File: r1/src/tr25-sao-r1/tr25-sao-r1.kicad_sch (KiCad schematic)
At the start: 1 part

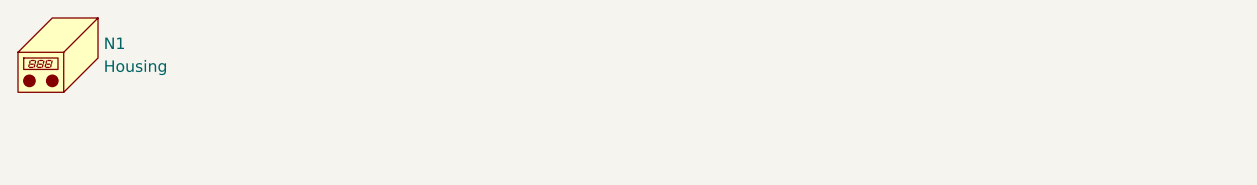
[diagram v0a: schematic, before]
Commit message: jeffmakes Kicad library as submodule
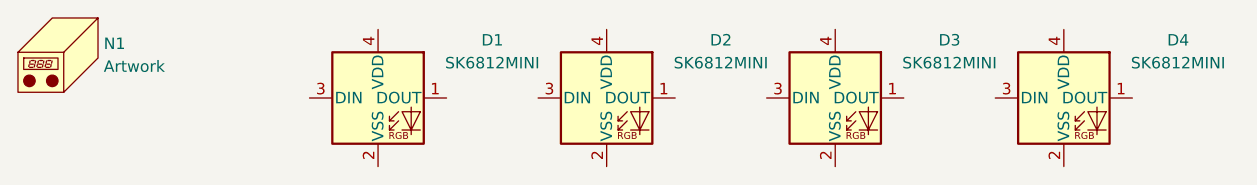
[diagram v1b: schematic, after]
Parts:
- added D1, D2, D3, D4: SK6812MINI, jeffmakes-footprints:LED_PLCC4_3.2x2.8mm_CCW, symbol LED:SK6812MINI
- N1: value Housing -> Artwork

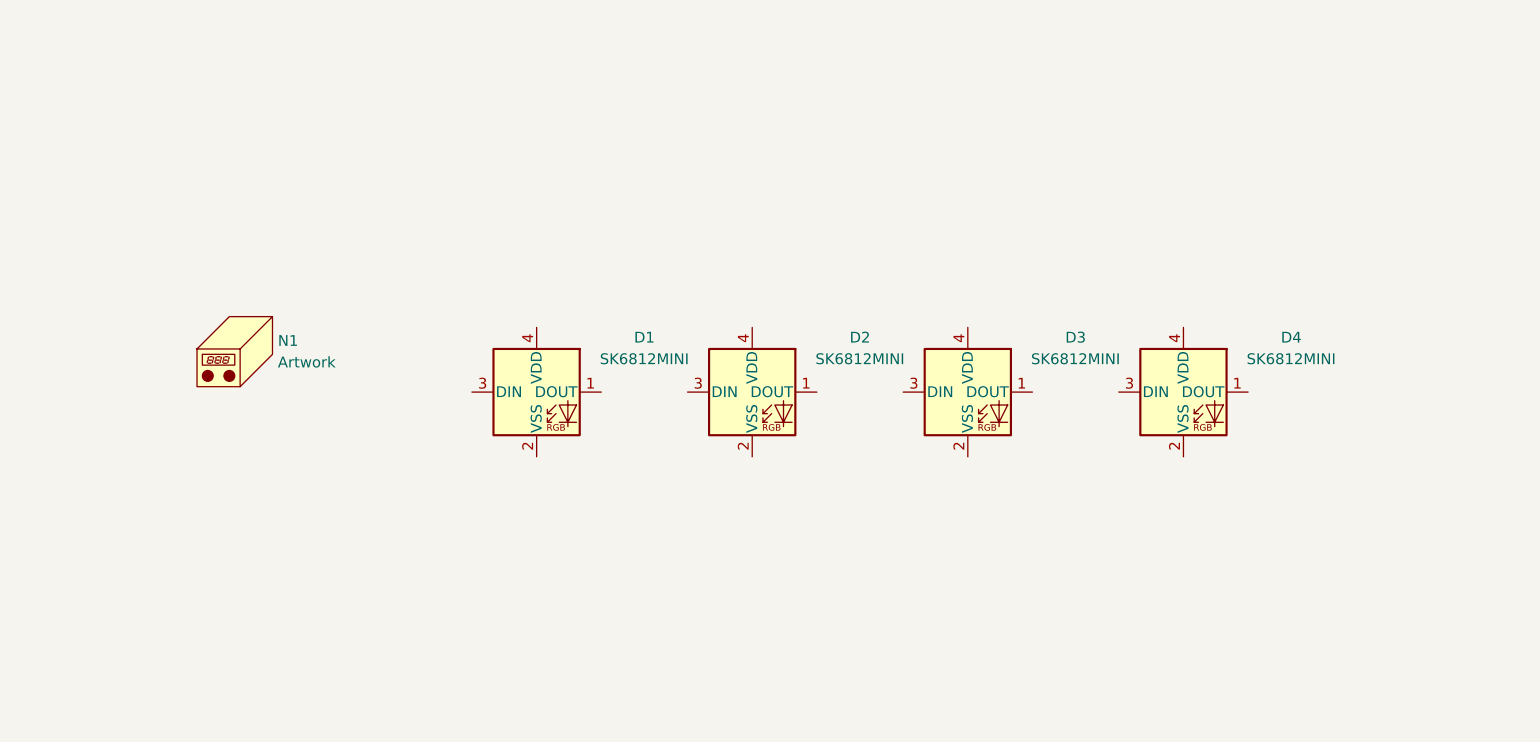
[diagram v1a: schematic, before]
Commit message: Schematic complete, ERC pass
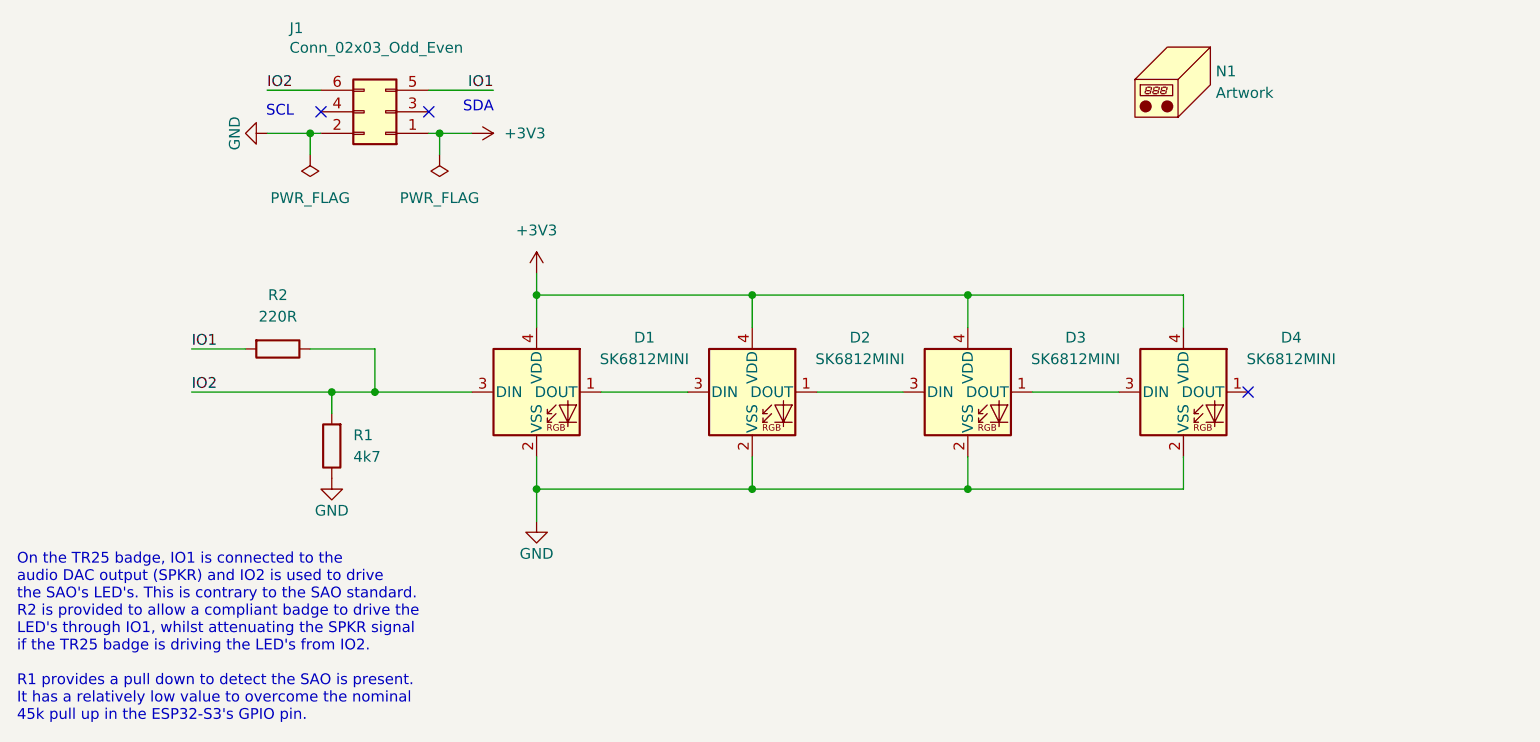
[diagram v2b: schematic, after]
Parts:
- added J1: Conn_02x03_Odd_Even, Connector_PinHeader_2.54mm:PinHeader_2x03_P2.54mm_Vertical_SMD, symbol Connector_Generic:Conn_02x03_Odd_Even
- added R1: 4k7, symbol Device:R
- added R2: 220R, symbol Device:R
- D1, D2, D3, D4: footprint jeffmakes-footprints:LED_PLCC4_3.2x2.8mm_CCW -> LED_SMD:LED_SK6812MINI_PLCC4_3.5x3.5mm_P1.75mm
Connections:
- net GND: now reaches D4.2 (VSS)
- net GND: now also D1.2 (VSS), D2.2 (VSS), D3.2 (VSS), J1.2 (Pin_2), R1.1
- net at D4.3 (DIN): now also D3.1 (DOUT)
- net +3V3: now reaches D4.4 (VDD)
- net +3V3: now also D1.4 (VDD), D2.4 (VDD), D3.4 (VDD), J1.1 (Pin_1)
- net at D1.1 (DOUT): now also D2.3 (DIN)
- net IO2: now reaches D1.3 (DIN)
- net IO2: now also J1.6 (Pin_6), R1.2, R2.1
- net at D3.3 (DIN): now also D2.1 (DOUT)
- new net IO1: J1.5 (Pin_5), R2.2
- no-connect marks 0 -> 3
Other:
- note added: "On the TR25 badge, IO1 is connected to the audio DAC output (SPKR) and IO2 is used to drive the SAO's LED's. This is contrary to the SAO standard. R2 is provided to allow a compliant badge to drive the LED's through IO1, whilst attenuating the SPKR signal if the TR25 badge is driving the LED's from IO2. R1 provides a pull down to detect the SAO is present. It has a relatively low value to overcom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"
- note added: "SCL"
- note added: "SDA"
- moved on the sheet: N1

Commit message: Assign resistor footprints
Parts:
- R1, R2: footprint (none) -> Resistor_SMD:R_1206_3216Metric
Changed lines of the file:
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@@
 			)
 		)
-		(property "Footprint" ""
+		(property "Footprint" "Resistor_SMD:R_1206_3216Metric"
 			(at 79.248 97.79 90)
 			(hide yes)
@@
 			)
 		)
-		(property "Footprint" ""
+		(property "Footprint" "Resistor_SMD:R_1206_3216Metric"
 			(at 71.12 84.582 90)
 			(hide yes)

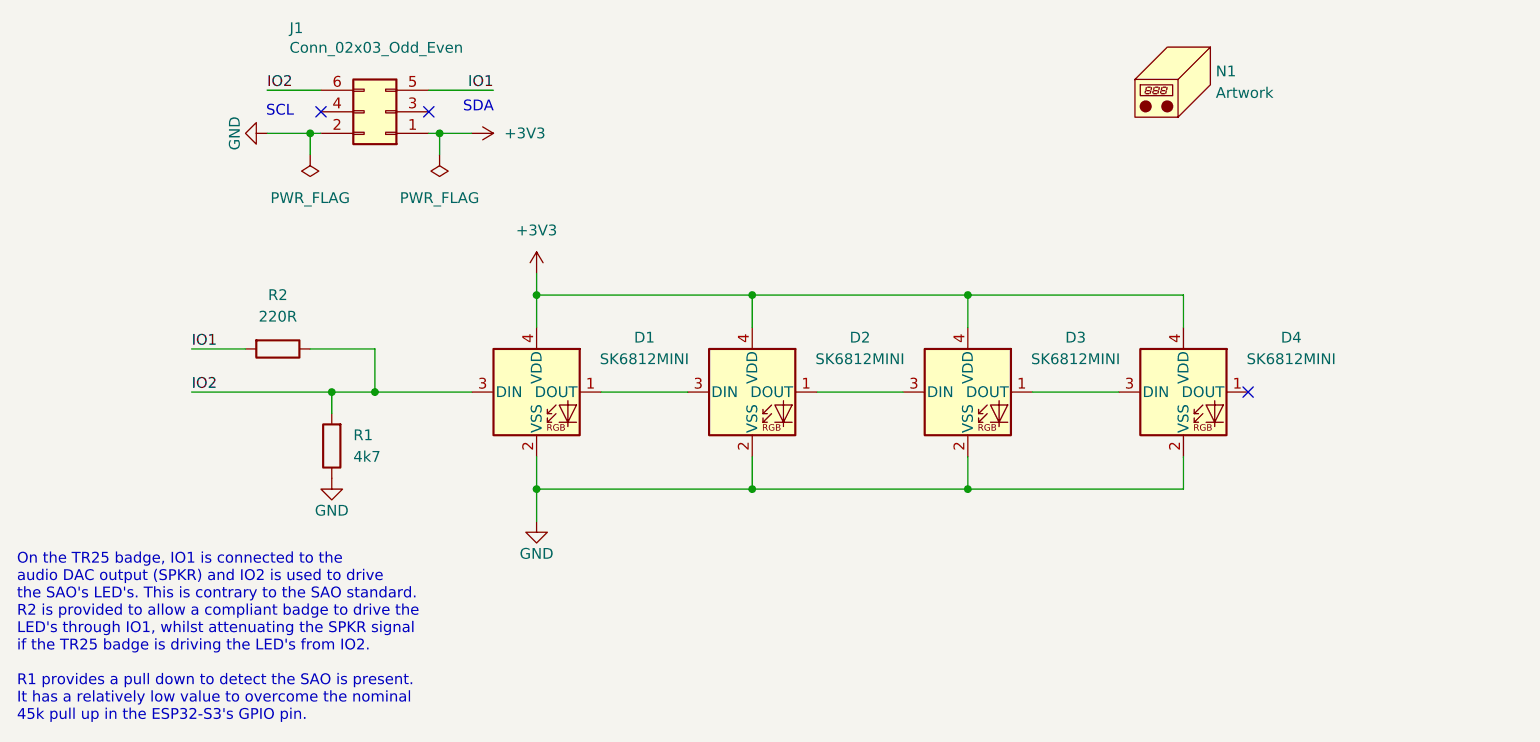
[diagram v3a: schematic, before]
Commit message: Correct LED pinout
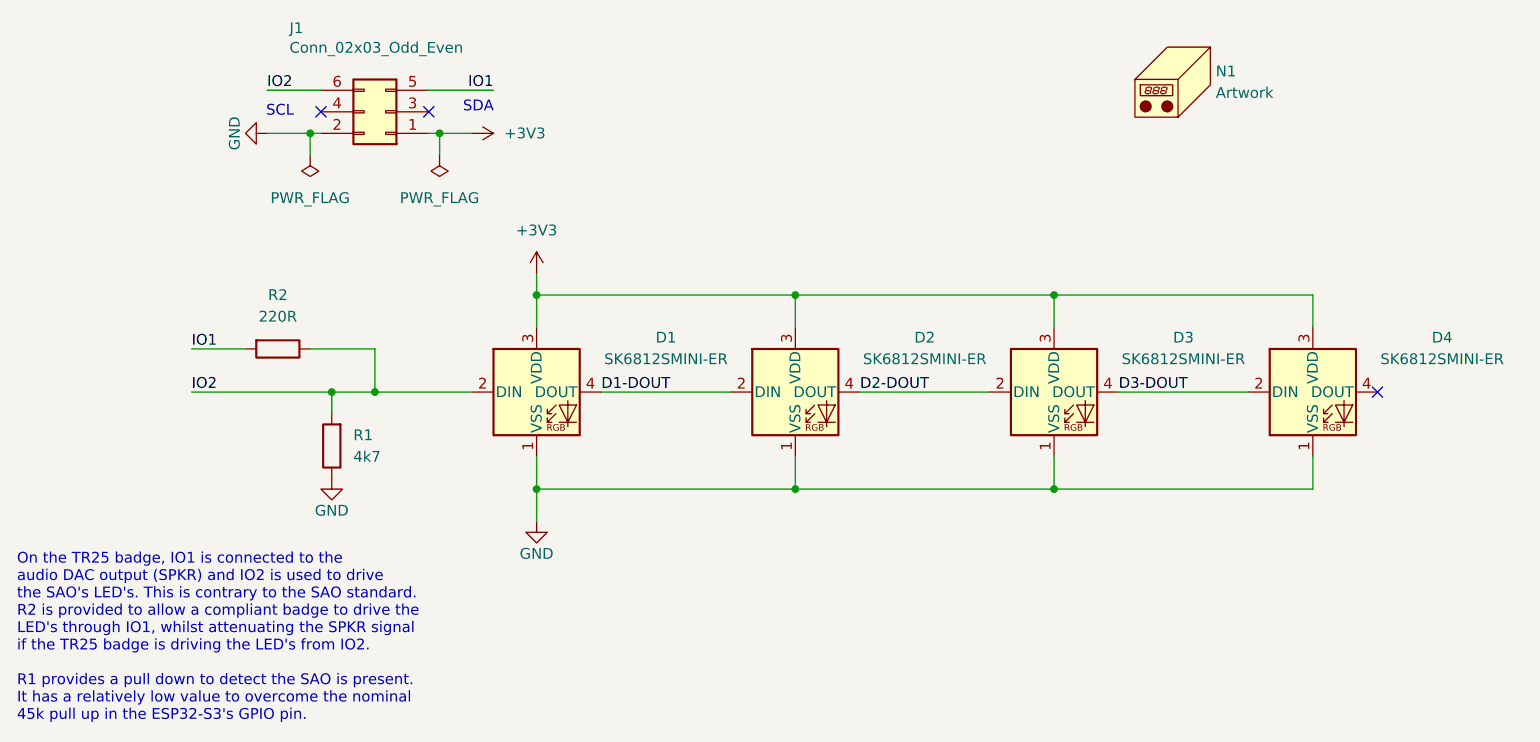
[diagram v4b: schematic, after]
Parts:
- D1, D2, D3, D4: value SK6812MINI -> SK6812SMINI-ER; footprint LED_SMD:LED_SK6812MINI_PLCC4_3.5x3.5mm_P1.75mm -> jeffmakes-footprints:LED_PLCC4_3.2x2.8mm_CCW; symbol LED:SK6812MINI -> j_LED:SK6812SMINI-ER
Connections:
- net +3V3: now also D1.3 (VDD), D2.3 (VDD), D3.3 (VDD), D4.3 (VDD); no longer D1.4 (VDD), D2.4 (VDD), D3.4 (VDD), D4.4 (VDD)
- net GND: now also D1.1 (VSS), D2.1 (VSS), D3.1 (VSS), D4.1 (VSS); no longer D1.2 (VSS), D2.2 (VSS), D3.2 (VSS), D4.2 (VSS)
- net IO2: now also D1.2 (DIN); no longer D1.3 (DIN)
- new net D1-DOUT: D1.4 (DOUT), D2.2 (DIN)
- new net D2-DOUT: D2.4 (DOUT), D3.2 (DIN)
- new net D3-DOUT: D3.4 (DOUT), D4.2 (DIN)
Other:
- moved on the sheet: D2, D3, D4

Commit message: Routing complete. DRC pass
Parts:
- R1: value 4k7 -> 4.7k
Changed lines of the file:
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@@
 			)
 		)
-		(property "Value" "4k7"
+		(property "Value" "4.7k"
 			(at 80.01 99.0599 0)
 			(effects
